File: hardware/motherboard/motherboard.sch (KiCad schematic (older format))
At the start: 84 parts, among them J1 Conn_01x04_Female, J10 Conn_01x02_Female, J11 Conn_01x02_Female, J12 Conn_01x03_Male, J13 Conn_01x03_Male, J14 Conn_01x03_Male, J15 Conn_01x06_Female, J16 Conn_01x02_Female, J17 Conn_01x03_Male, J18 Conn_01x01_Female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

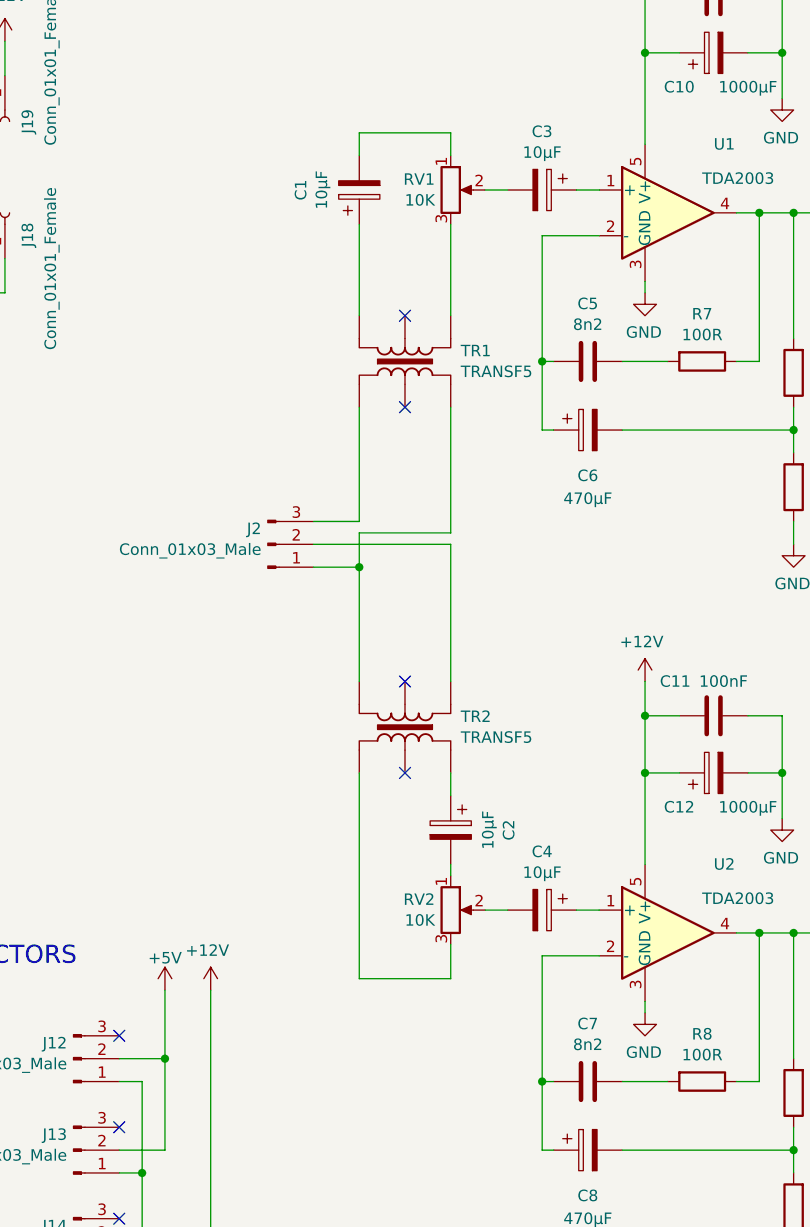
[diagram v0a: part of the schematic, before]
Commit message: adjusted heatsink
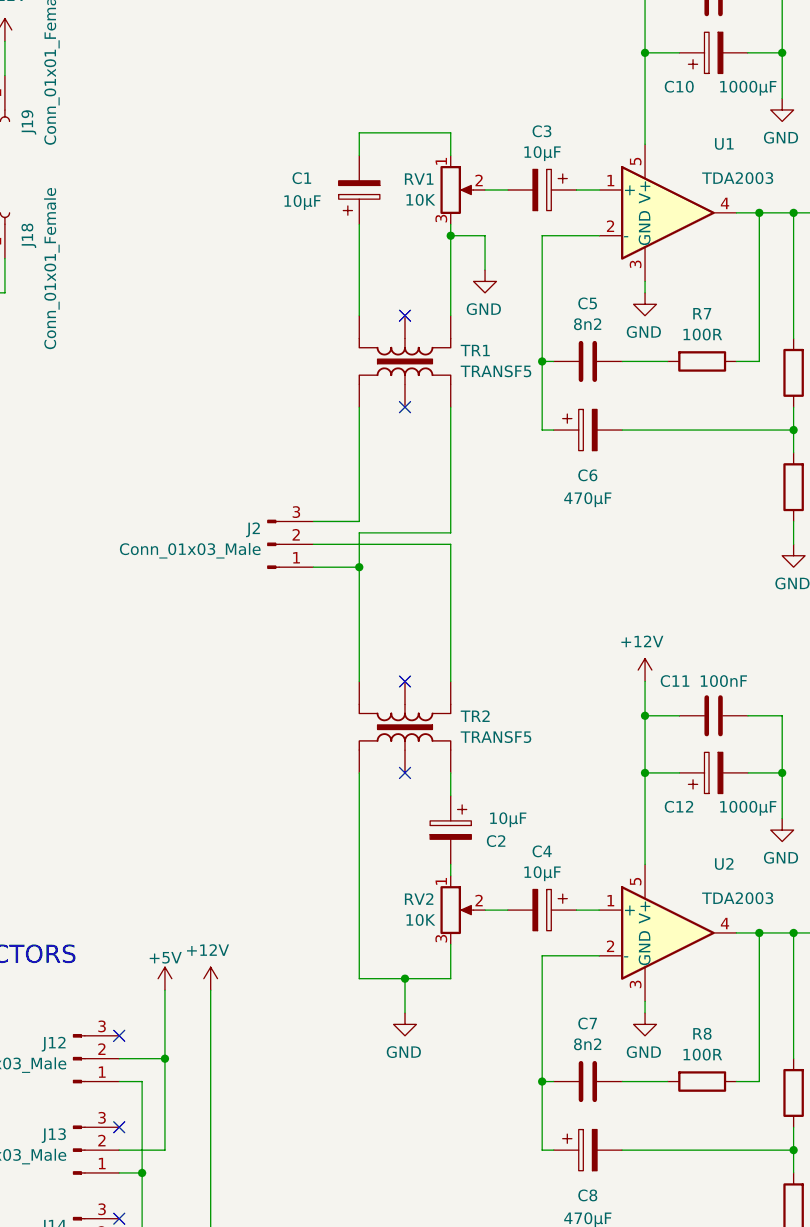
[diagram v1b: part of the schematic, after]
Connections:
- net GND: now also RV1.3, RV2.3, TR1.4, TR2.4
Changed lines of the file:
@@
 U 1 1 602F12BB
 P 11300 4850
-F 0 "C2" V 11045 4850 50  0000 C CNN
-F 1 "10µF" V 11136 4850 50  0000 C CNN
+F 0 "C2" H 11100 4800 50  0000 C CNN
+F 1 "10µF" H 11050 4900 50  0000 C CNN
 F 2 "Capacitor_THT:CP_Radial_D6.3mm_P2.50mm" H 11338 4700 50  0001 C CNN
 F 3 "~" H 11300 4850 50  0001 C CNN
@@
 U 1 1 5FFE3845
 P 10900 2050
-F 0 "C1" V 10645 2050 50  0000 C CNN
-F 1 "10µF" V 10736 2050 50  0000 C CNN
+F 0 "C1" H 10650 2000 50  0000 C CNN
+F 1 "10µF" H 10650 2100 50  0000 C CNN
 F 2 "Capacitor_THT:CP_Radial_D6.3mm_P2.50mm" H 10938 1900 50  0001 C CNN
 F 3 "~" H 10900 2050 50  0001 C CNN
@@
 $EndComp
 Wire Wire Line
-	10900 5500 11300 5500
+	10900 5500 11100 5500
 Wire Wire Line
 	11300 5350 11300 5500
@@
 	10900 2200 10900 2600
 Wire Wire Line
-	11300 2200 11300 2600
+	11300 2200 11300 2250
 Wire Wire Line
 	10900 4600 10900 5500
@@
 Wire Wire Line
 	9350 2350 9350 2500
+$Comp
+L power:GND #PWR0136
+U 1 1 5FADD11F
+P 11100 5650
+F 0 "#PWR0136" H 11100 5400 50  0001 C CNN
+F 1 "GND" H 11105 5477 50  0000 C CNN
+F 2 "" H 11100 5650 50  0001 C CNN
+F 3 "" H 11100 5650 50  0001 C CNN
+	1    11100 5650
+	-1   0    0    -1
+$EndComp
+Wire Wire Line
+	11100 5650 11100 5500
+Connection ~ 11100 5500
+Wire Wire Line
+	11100 5500 11300 5500
+$Comp
+L power:GND #PWR0137
+U 1 1 5FB00584
+P 11450 2400
+F 0 "#PWR0137" H 11450 2150 50  0001 C CNN
+F 1 "GND" H 11455 2227 50  0000 C CNN
+F 2 "" H 11450 2400 50  0001 C CNN
+F 3 "" H 11450 2400 50  0001 C CNN
+	1    11450 2400
+	-1   0    0    -1
+$EndComp
+Wire Wire Line
+	11450 2400 11450 2250
+Wire Wire Line
+	11450 2250 11300 2250
+Connection ~ 11300 2250
+Wire Wire Line
+	11300 2250 11300 2600
 $EndSCHEMATC

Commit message: hardware revision 0.3
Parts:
- removed D1: 1N4148W, Diode_SMD:D_SOD-128, symbol Diode:1N4148W
- removed D8: LED, LED_SMD:LED_1210_3225Metric_Pad1.42x2.65mm_HandSolder, symbol Device:LED
- removed K2: SANYOU_SRD_Form_C, Relay_THT:Relay_SPDT_SANYOU_SRD_Series_Form_C, symbol Relay:SANYOU_SRD_Form_C
- removed Q1, Q2, Q3, Q4, Q5: BSS138, Package_TO_SOT_SMD:SOT-23_Handsoldering, symbol Transistor_FET:BSS138
- removed R15, R23, R3: 10K, Resistor_SMD:R_1210_3225Metric_Pad1.42x2.65mm_HandSolder, symbol Device:R
- removed R20: ?, Resistor_SMD:R_1210_3225Metric_Pad1.42x2.65mm_HandSolder, symbol Device:R
- added U3: 74HCT125, Package_DIP:DIP-14_W7.62mm_Socket_LongPads, symbol 74hct125:74HCT125
- R17: value 10K -> 5.1K
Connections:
- net +3V3: no longer R17.1
- net +5V: now also U3.14 (VCC); no longer R16.2, R5.2, R6.2
- net GND: now also R16.2, R5.2, R6.2, U3.12 (4A), U3.2 (1A), U3.5 (2A), U3.7 (GND), U3.9 (3A)
- net GPIO11(SPI0_SCK): no longer R21.2
- net GPIO12(PWM0): now also R16.1, R18.2, U3.4 (2~OE); no longer R19.1, R25.2
- net GPIO13(PWM1): no longer R24.2
- net GPIO16: now also R17.1, R5.1; no longer R17.2
- net GPIO18(GEN1)(PWM0): now also R22.1, R25.2, U3.13 (4~OE)
- net GPIO19(SPI1_MISO): now also R21.2, R6.1, U3.1 (1~OE); no longer R18.2, R22.1
- net GPIO21(SPI1_SCK): now also R19.1, R24.2, U3.10 (3~OE)
- net at J4.1 (Pin_1): now also J18.1 (Pin_1)
- net MOTOR_VR: now reaches J5.2 (Pin_2)
- net MOTOR_VR: now also U3.6 (2Y); no longer R16.1
- net at J5.4 (Pin_4): now also R17.2; no longer R5.1
- net MOTOR_EL: now reaches J5.5 (Pin_5)
- net MOTOR_EL: now also U3.3 (1Y)
- net at J16.2 (Pin_2): now also U3.11 (4Y)
- net at J8.2 (Pin_2): now also U3.8 (3Y); no longer R6.1
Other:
- note added: "LOGIC SHIFTER"
- note removed: "EXPOSED GPIO"
- moved on the sheet: D5, D6, D7, D9, J1, J12, J13, J14, J15, J16, J17, J18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

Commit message: hardware v0.3
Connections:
- net GND: now also U3.1 (1~OE), U3.10 (3~OE), U3.13 (4~OE), U3.4 (2~OE); no longer U3.12 (4A), U3.2 (1A), U3.5 (2A), U3.9 (3A)
- net GPIO12(PWM0): now also U3.5 (2A); no longer U3.4 (2~OE)
- net GPIO18(GEN1)(PWM0): now also U3.12 (4A); no longer U3.13 (4~OE)
- net GPIO19(SPI1_MISO): now also U3.2 (1A); no longer U3.1 (1~OE)
- net GPIO21(SPI1_SCK): now also U3.9 (3A); no longer U3.10 (3~OE)
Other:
- moved on the sheet: R16, R19, R22, R6
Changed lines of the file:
@@
 Wire Wire Line
 	11300 2250 11300 2600
-Text Label 3950 8200 0    50   ~ 0
+Text Label 3950 8100 0    50   ~ 0
 GPIO18(GEN1)(PWM0)
 $Comp
@@
 	1    0    0    -1
 $EndComp
-Text Label 3950 7800 0    50   ~ 0
+Text Label 3950 7700 0    50   ~ 0
 GPIO12(PWM0)
 $Comp
@@
 	5450 8550 5450 8500
 Wire Wire Line
-	4950 7500 4850 7500
-Wire Wire Line
-	4850 7500 4850 7700
+	4950 7600 4850 7600
 Wire Wire Line
 	4850 8500 5450 8500
@@
 	5450 8500 5450 8450
 Wire Wire Line
-	4950 7700 4850 7700
-Connection ~ 4850 7700
-Wire Wire Line
-	4850 7700 4850 7900
-Wire Wire Line
-	4950 7900 4850 7900
-Connection ~ 4850 7900
-Wire Wire Line
-	4850 7900 4850 8100
-Wire Wire Line
-	4950 8100 4850 8100
-Connection ~ 4850 8100
-Wire Wire Line
-	4850 8100 4850 8500
+	4950 7800 4850 7800
+Wire Wire Line
+	4950 8000 4850 8000
+Wire Wire Line
+	4950 8200 4850 8200
 $Comp
 L Connector:Conn_01x02_Female J8
@@
 Wire Wire Line
 	6450 8100 6450 7800
-Text Label 3950 7600 0    50   ~ 0
+Text Label 3950 7500 0    50   ~ 0
 GPIO19(SPI1_MISO)
 Text Label 6750 7600 2    50   ~ 0
@@
 Wire Wire Line
 	5650 2200 5650 3450
-Text Label 3950 8000 0    50   ~ 0
+Text Label 3950 7900 0    50   ~ 0
 GPIO21(SPI1_SCK)
 $Comp
@@
 L Device:R R6
 U 1 1 6064C4DB
-P 3650 7600
-F 0 "R6" V 3750 7500 50  0000 C CNN
-F 1 "10K" V 3750 7700 50  0000 C CNN
-F 2 "Resistor_SMD:R_1210_3225Metric_Pad1.42x2.65mm_HandSolder" V 3580 7600 50  0001 C CNN
-F 3 "~" H 3650 7600 50  0001 C CNN
-	1    3650 7600
-	0    1    1    0
-$EndComp
-Wire Wire Line
-	3800 7600 4950 7600
+P 3650 7500
+F 0 "R6" V 3750 7400 50  0000 C CNN
+F 1 "10K" V 3750 7600 50  0000 C CNN
+F 2 "Resistor_SMD:R_1210_3225Metric_Pad1.42x2.65mm_HandSolder" V 3580 7500 50  0001 C CNN
+F 3 "~" H 3650 7500 50  0001 C CNN
+	1    3650 7500
+	0    1    1    0
+$EndComp
+Wire Wire Line
+	3800 7500 4950 7500
 $Comp
 L Device:R R16
 U 1 1 60668168
-P 3650 7800
-F 0 "R16" V 3750 7700 50  0000 C CNN
-F 1 "10K" V 3750 7900 50  0000 C CNN
-F 2 "Resistor_SMD:R_1210_3225Metric_Pad1.42x2.65mm_HandSolder" V 3580 7800 50  0001 C CNN
-F 3 "~" H 3650 7800 50  0001 C CNN
-	1    3650 7800
+P 3650 7700
+F 0 "R16" V 3750 7600 50  0000 C CNN
+F 1 "10K" V 3750 7800 50  0000 C CNN
+F 2 "Resistor_SMD:R_1210_3225Metric_Pad1.42x2.65mm_HandSolder" V 3580 7700 50  0001 C CNN
+F 3 "~" H 3650 7700 50  0001 C CNN
+	1    3650 7700
 	0    1    1    0
 $EndComp
@@
 L Device:R R19
 U 1 1 60668396
-P 3650 8000
-F 0 "R19" V 3750 7900 50  0000 C CNN
-F 1 "10K" V 3750 8100 50  0000 C CNN
-F 2 "Resistor_SMD:R_1210_3225Metric_Pad1.42x2.65mm_HandSolder" V 3580 8000 50  0001 C CNN
-F 3 "~" H 3650 8000 50  0001 C CNN
-	1    3650 8000
+P 3650 7900
+F 0 "R19" V 3750 7800 50  0000 C CNN
+F 1 "10K" V 3750 8000 50  0000 C CNN
+F 2 "Resistor_SMD:R_1210_3225Metric_Pad1.42x2.65mm_HandSolder" V 3580 7900 50  0001 C CNN
+F 3 "~" H 3650 7900 50  0001 C CNN
+	1    3650 7900
 	0    1    1    0
 $EndComp
@@
 L Device:R R22
 U 1 1 606685E1
-P 3650 8200
-F 0 "R22" V 3750 8100 50  0000 C CNN
-F 1 "10K" V 3750 8300 50  0000 C CNN
-F 2 "Resistor_SMD:R_1210_3225Metric_Pad1.42x2.65mm_HandSolder" V 3580 8200 50  0001 C CNN
-F 3 "~" H 3650 8200 50  0001 C CNN
-	1    3650 8200
+P 3650 8100
+F 0 "R22" V 3750 8000 50  0000 C CNN
+F 1 "10K" V 3750 8200 50  0000 C CNN
+F 2 "Resistor_SMD:R_1210_3225Metric_Pad1.42x2.65mm_HandSolder" V 3580 8100 50  0001 C CNN
+F 3 "~" H 3650 8100 50  0001 C CNN
+	1    3650 8100
 	0    1    1    0
 $EndComp
@@
 L power:GND #PWR0133
 U 1 1 60668BDD
-P 3300 8550
-F 0 "#PWR0133" H 3300 8300 50  0001 C CNN
-F 1 "GND" H 3305 8377 50  0000 C CNN
-F 2 "" H 3300 8550 50  0001 C CNN
-F 3 "" H 3300 8550 50  0001 C CNN
-	1    3300 8550
-	-1   0    0    -1
-$EndComp
-Wire Wire Line
-	3300 8550 3300 8200
-Wire Wire Line
-	3300 8200 3500 8200
-Wire Wire Line
-	3300 8200 3300 8000
-Wire Wire Line
-	3300 8000 3500 8000
-Connection ~ 3300 8200
-Wire Wire Line
-	3500 7800 3300 7800
-Wire Wire Line
-	3300 7800 3300 8000
-Connection ~ 3300 8000
-Wire Wire Line
-	3300 7800 3300 7600
-Wire Wire Line
-	3300 7600 3500 7600
-Connection ~ 3300 7800
-Wire Wire Line
-	3800 8200 4950 8200
-Wire Wire Line
-	3800 8000 4950 8000
-Wire Wire Line
-	3800 7800 4950 7800
+P 3300 8450
+F 0 "#PWR0133" H 3300 8200 50  0001 C CNN
+F 1 "GND" H 3305 8277 50  0000 C CNN
+F 2 "" H 3300 8450 50  0001 C CNN
+F 3 "" H 3300 8450 50  0001 C CNN
+	1    3300 8450
+	-1   0    0    -1
+$EndComp
+Wire Wire Line
+	3300 8450 3300 8100
+Wire Wire Line
+	3300 8100 3500 8100
+Wire Wire Line
+	3300 8100 3300 7900
+Wire Wire Line
+	3300 7900 3500 7900
+Connection ~ 3300 8100
+Wire Wire Line
+	3500 7700 3300 7700
+Wire Wire Line
+	3300 7700 3300 7900
+Connection ~ 3300 7900
+Wire Wire Line
+	3300 7700 3300 7500
+Wire Wire Line
+	3300 7500 3500 7500
+Connection ~ 3300 7700
+Wire Wire Line
+	3800 8100 4950 8100
+Wire Wire Line
+	3800 7900 4950 7900
+Wire Wire Line
+	3800 7700 4950 7700
 $Comp
 L Connector:Conn_01x05_Female J7
@@
 Wire Wire Line
 	6050 4450 7100 4450
+Connection ~ 4850 7800
+Connection ~ 4850 8000
+Connection ~ 4850 8200
+Wire Wire Line
+	4850 8200 4850 8500
+Wire Wire Line
+	4850 7600 4850 7800
+Wire Wire Line
+	4850 7800 4850 8000
+Wire Wire Line
+	4850 8000 4850 8200
 $EndSCHEMATC
